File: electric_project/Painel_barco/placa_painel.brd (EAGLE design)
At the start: 60 x 100 mm, 15 parts, among them IC1 7805TV

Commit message: up
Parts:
- removed R3, R4: (no value), rcl:0204/7
- removed X2: (no value), con-molex-micro-fit-3_0:43045-1012
- added BB, BE: (no value), con-ptr500:AK500/3
- added BB_IN, BE_IN, DMS: (no value), con-ptr500:AK500/2
- added MOTOR_CON: (no value), con-molex-micro-fit-3_0:43045-1012
- moved R2 22.8 mm to (40.8, 41.0), turned to 270 degrees
- moved IC2 16.6 mm to (30.5, 50.8), turned to 0 degrees
- moved C2 4.58 mm to (33.0, 67.3)
- moved R1 4.02 mm to (22.9, 33.0), turned to 270 degrees
- moved X3 3.81 mm to (9.40, 53.7)
- moved X7 3.81 mm to (9.40, 65.8)
- moved C1 3.59 mm to (24.1, 67.3)
- moved IC1 1.80 mm to (26.7, 76.2)
- moved REV 1.80 mm to (52.1, 39.4)
- moved ON_OFF 1.27 mm to (52.1, 25.4)
- moved POT 1.27 mm to (52.1, 10.2)
- renumbered X1 to TELE_CON
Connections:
- removed net BB_IN: TELE_CON.P$12
- removed net BE_IN: TELE_CON.P$1
- removed net DMS_IN: TELE_CON.P$7
- removed net N$8: R3.1, R4.2
- new net BB_AUTO: BB.1, BB_IN.2
- new net BB_RET: BB.2, BB_IN.1, TELE_CON.P$12
- new net BE_AUTO: BE.1, BE_IN.2
- new net BE_RET: BE.2, BE_IN.1, TELE_CON.P$1
- new net WHITE_DMS: DMS.2, MOTOR_CON.P$1, TELE_CON.P$7
- net 21: now also X7.P$4; no longer X7.P$3
- net 22: now also X7.P$2; no longer X7.P$4
- net BLACK_GND: now also MOTOR_CON.P$10, MOTOR_CON.P$8; no longer X2.P$10, X2.P$8
- net BLUE_5V: now also MOTOR_CON.P$6; no longer X2.P$6
- net BROWN_REVERSE: now also MOTOR_CON.P$2; no longer X2.P$2
- net GND: now also DMS.1, MOTOR_CON.P$4, MOTOR_CON.P$5; no longer R4.1, X2.P$4, X2.P$5
- net PURP_45V_ONOFF_BACK: now also MOTOR_CON.P$3; no longer R3.2, X2.P$3
- net RED_ONOFF_45V_PH: now also MOTOR_CON.P$9; no longer X2.P$9
- net VCC_12: now also BB.3, BE.3
- net VCC_5V: now also X7.P$3; no longer X7.P$2
- net WHITE_CRUISE: no longer X2.P$1
- net YEL_POT_MEASURE: now also MOTOR_CON.P$7; no longer X2.P$7
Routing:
- net GND: track 0.00 -> 250.3 mm
- net BE_RET: track 0.00 -> 246.9 mm
- net BB_RET: track 0.00 -> 213.9 mm
- net WHITE_DMS: track 0.00 -> 165.0 mm
- net VCC_12: track 0.00 -> 118.5 mm
- net BLACK_GND: track 0.00 -> 89.7 mm
- net BROWN_REVERSE: track 0.00 -> 74.1 mm
- net BE_AUTO: track 0.00 -> 58.7 mm
- net ONOFF_MOTOR: track 0.00 -> 56.6 mm
- net PURP_45V_ONOFF_BACK: track 0.00 -> 54.4 mm
- net BB_AUTO: track 0.00 -> 50.5 mm
- net VCC_5V: track 0.00 -> 43.8 mm
- net 21: track 0.00 -> 41.2 mm
- net RED_ONOFF_45V_PH: track 0.00 -> 39.0 mm
- net BLUE_5V: track 0.00 -> 36.3 mm
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
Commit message: up
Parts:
- moved TELE_CON 3.81 mm to (9.40, 36.1)
- moved MOTOR_CON 1.27 mm to (13.2, 13.5)
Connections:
- removed net GND: C1.-, C2.-, DMS.1, IC1.2, IC2.7, MOTOR_CON.P$4, MOTOR_CON.P$5, R2.1, REV.1, X3.P$1, X7.P$1
- removed net N$1: TELE_CON.P$5
- removed net N$2: TELE_CON.P$3
- net 21: now also TELE_CON.P$3
- net 22: now also TELE_CON.P$5
- net BLACK_GND: now also C1.-, C2.-, DMS.1, IC1.2, IC2.7, MOTOR_CON.P$3, MOTOR_CON.P$4, MOTOR_CON.P$5, R2.1, REV.1, X3.P$1, X7.P$1; no longer MOTOR_CON.P$10
- net BROWN_REVERSE: now also MOTOR_CON.P$1; no longer MOTOR_CON.P$2
- net PURP_45V_ONOFF_BACK: now also MOTOR_CON.P$10; no longer MOTOR_CON.P$3
- net WHITE_DMS: now also MOTOR_CON.P$2; no longer MOTOR_CON.P$1
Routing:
- net GND: track 250.3 -> 0.00 mm
- net BLACK_GND: track 89.7 -> 257.4 mm
- net BE_RET: track 246.9 -> 127.3 mm, vias 0 -> 2
- net BB_RET: track 213.9 -> 99.5 mm, vias 0 -> 2
- net YEL_POT_MEASURE: track 36.3 -> 81.4 mm, vias 0 -> 2
- net PURP_45V_ONOFF_BACK: track 54.4 -> 43.1 mm
- net VCC_12: track 118.5 -> 108.8 mm
- net 21: track 41.2 -> 48.3 mm
- net WHITE_DMS: track 165.0 -> 159.3 mm
- net BROWN_REVERSE: track 74.1 -> 69.9 mm
- net 22: track 27.2 -> 31.2 mm
- net ONOFF_MOTOR: track 56.6 -> 54.1 mm
- net BLUE_5V: track 36.3 -> 37.0 mm
- net RED_ONOFF_45V_PH: track 39.0 -> 38.5 mm

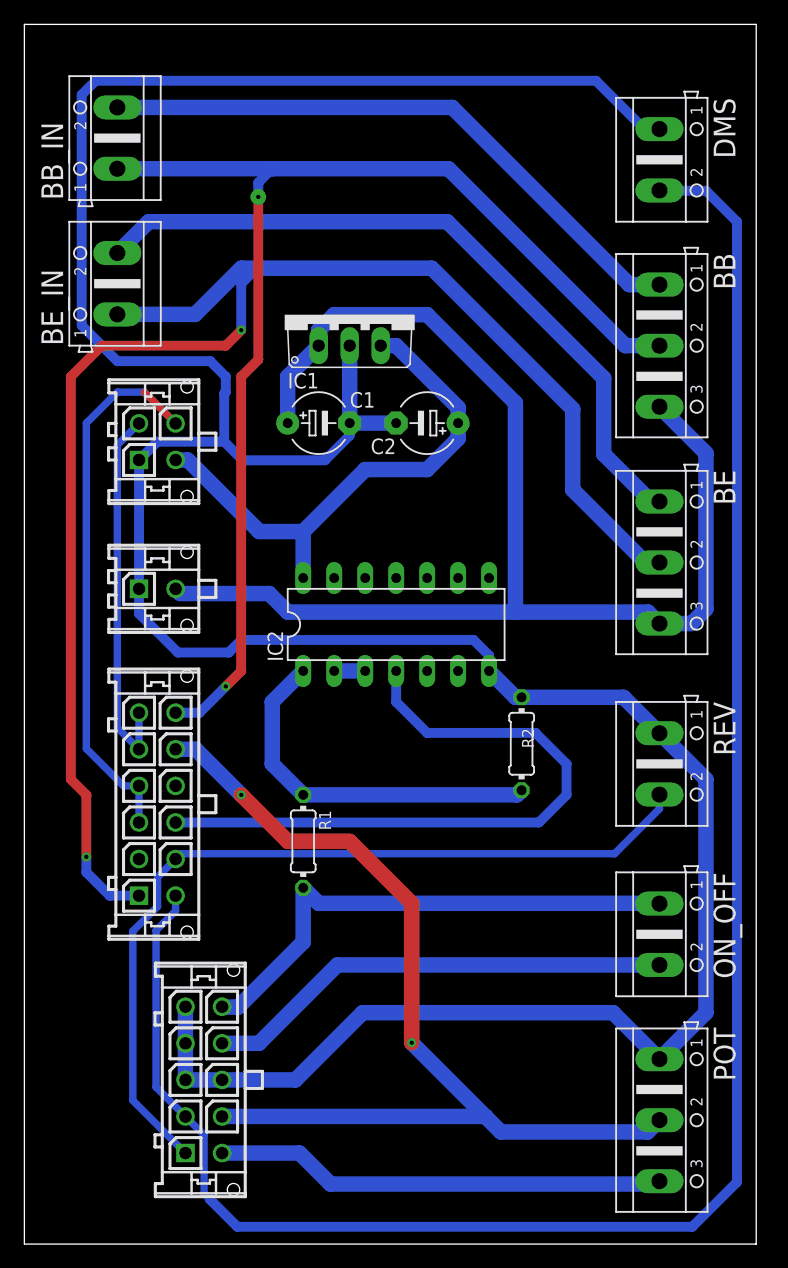
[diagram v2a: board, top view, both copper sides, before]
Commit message: increased of vias diameter
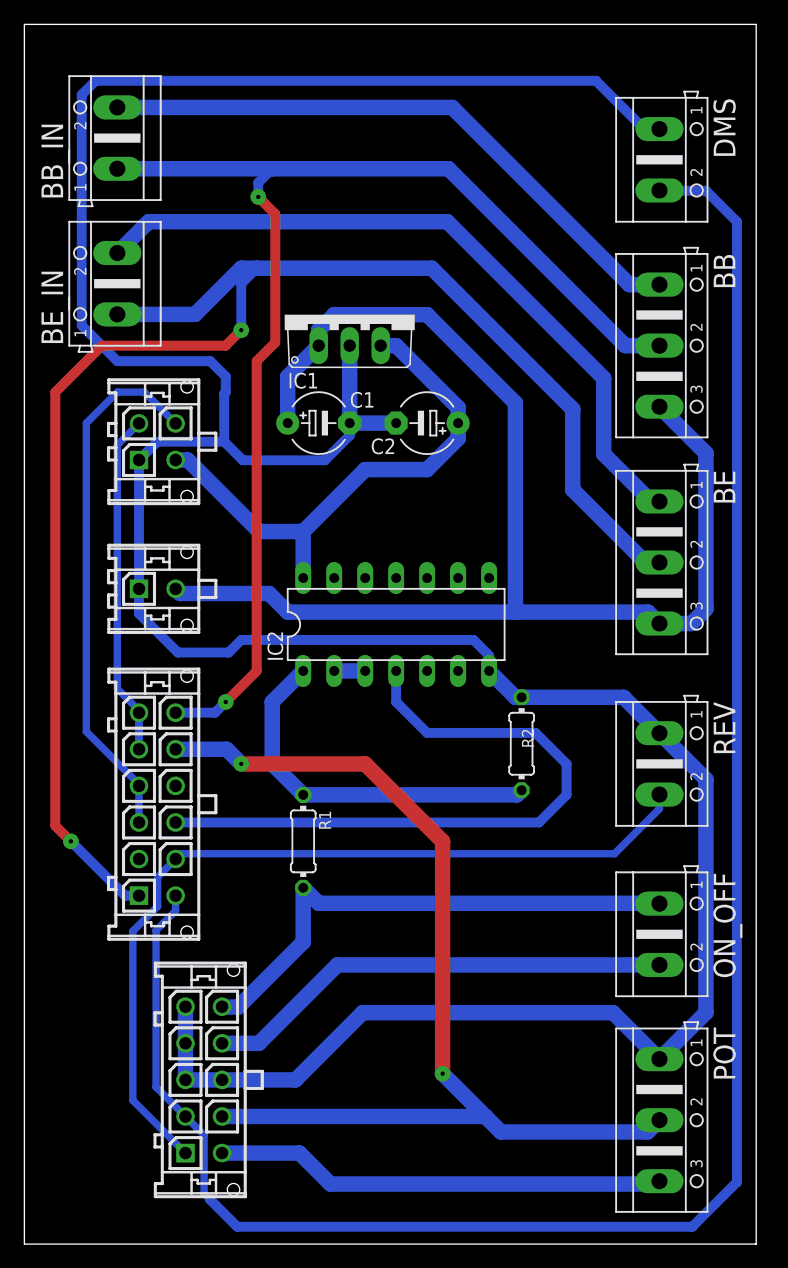
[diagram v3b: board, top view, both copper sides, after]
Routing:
- net YEL_POT_MEASURE: track 81.4 -> 85.8 mm
- net 21: track 48.3 -> 44.0 mm
- net BB_RET: track 99.5 -> 101.4 mm
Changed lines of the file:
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@@
 <?xml version="1.0" encoding="utf-8"?>
 <!DOCTYPE eagle SYSTEM "eagle.dtd">
-<eagle version="9.4.2">
+<eagle version="9.5.0">
 <drawing>
 <settings>
-<setting alwaysvectorfont="yes"/>
+<setting alwaysvectorfont="no"/>
 <setting verticaltext="up"/>
 </settings>
@@
 <contactref element="TELE_CON" pad="P$5"/>
 <wire x1="9.398" y1="40.568" x2="9.398" y2="43.568" width="0.6096" layer="16"/>
-<wire x1="9.398" y1="40.568" x2="7.62" y2="42.346" width="0.6096" layer="16"/>
+<wire x1="9.398" y1="40.568" x2="9.398" y2="43.743" width="0.6096" layer="16"/>
+<wire x1="9.398" y1="43.743" x2="7.62" y2="45.521" width="0.6096" layer="16"/>
 <wire x1="7.62" y1="65.508" x2="9.398" y2="67.286" width="0.6096" layer="16"/>
-<wire x1="7.62" y1="42.346" x2="7.62" y2="65.508" width="0.6096" layer="16"/>
+<wire x1="7.62" y1="45.521" x2="7.62" y2="65.508" width="0.6096" layer="16"/>
 </signal>
 <signal name="21">
 <contactref element="TELE_CON" pad="P$4"/>
 <contactref element="X7" pad="P$4"/>
-<wire x1="9.834" y1="69.85" x2="12.398" y2="67.286" width="0.6096" layer="1"/>
 <contactref element="TELE_CON" pad="P$3"/>
+<wire x1="9.834" y1="69.85" x2="7.62" y2="69.85" width="0.6096" layer="16"/>
+<wire x1="9.398" y1="37.568" x2="9.398" y2="37.695" width="0.6096" layer="16"/>
+<wire x1="9.398" y1="37.695" x2="5.08" y2="42.013" width="0.6096" layer="16"/>
+<wire x1="7.62" y1="69.85" x2="5.08" y2="67.31" width="0.6096" layer="16"/>
+<wire x1="5.08" y1="67.31" x2="5.08" y2="42.013" width="0.6096" layer="16"/>
+<wire x1="9.398" y1="34.568" x2="9.398" y2="37.568" width="0.6096" layer="16"/>
 <wire x1="12.398" y1="67.286" x2="9.834" y2="69.85" width="0.6096" layer="16"/>
-<wire x1="9.834" y1="69.85" x2="7.62" y2="69.85" width="0.6096" layer="16"/>
-<wire x1="8.128" y1="37.568" x2="9.398" y2="37.568" width="0.6096" layer="16"/>
-<wire x1="8.128" y1="37.568" x2="5.08" y2="40.616" width="0.6096" layer="16"/>
-<wire x1="7.62" y1="69.85" x2="5.08" y2="67.31" width="0.6096" layer="16"/>
-<wire x1="5.08" y1="67.31" x2="5.08" y2="40.616" width="0.6096" layer="16"/>
-<wire x1="9.398" y1="34.568" x2="9.398" y2="37.568" width="0.6096" layer="16"/>
 </signal>
 <signal name="EXTRA2">
@@
 <wire x1="51.102" y1="9.192" x2="39.068" y2="9.192" width="1.27" layer="16"/>
 <wire x1="37.798" y1="10.462" x2="16.51" y2="10.462" width="1.27" layer="16"/>
-<wire x1="12.398" y1="40.568" x2="14.042" y2="40.568" width="1.27" layer="16"/>
-<wire x1="14.042" y1="40.568" x2="17.78" y2="36.83" width="1.27" layer="16"/>
-<via x="17.78" y="36.83" extent="1-16" drill="0.35"/>
-<wire x1="17.78" y1="36.83" x2="21.59" y2="33.02" width="1.27" layer="1"/>
-<wire x1="31.75" y1="27.94" x2="31.75" y2="16.51" width="1.27" layer="1"/>
-<via x="31.75" y="16.51" extent="1-16" drill="0.35"/>
-<wire x1="31.75" y1="16.51" x2="37.798" y2="10.462" width="1.27" layer="16"/>
+<wire x1="12.398" y1="40.568" x2="16.582" y2="40.568" width="1.27" layer="16"/>
+<wire x1="16.582" y1="40.568" x2="17.78" y2="39.37" width="1.27" layer="16"/>
+<via x="17.78" y="39.37" extent="1-16" drill="0.35" diameter="1.3"/>
+<wire x1="34.29" y1="33.02" x2="34.29" y2="13.97" width="1.27" layer="1"/>
+<via x="34.29" y="13.97" extent="1-16" drill="0.35" diameter="1.3"/>
+<wire x1="34.29" y1="13.97" x2="37.798" y2="10.462" width="1.27" layer="16"/>
 <wire x1="37.798" y1="10.462" x2="39.068" y2="9.192" width="1.27" layer="16"/>
-<wire x1="21.59" y1="33.02" x2="26.67" y2="33.02" width="1.27" layer="1"/>
-<wire x1="26.67" y1="33.02" x2="31.75" y2="27.94" width="1.27" layer="1"/>
+<wire x1="27.94" y1="39.37" x2="17.78" y2="39.37" width="1.27" layer="1"/>
+<wire x1="27.94" y1="39.37" x2="34.29" y2="33.02" width="1.27" layer="1"/>
 </signal>
 <signal name="WHITE_CRUISE">
@@
 <wire x1="49.276" y1="73.66" x2="52.07" y2="73.66" width="1.27" layer="16"/>
 <wire x1="34.7726" y1="88.1634" x2="49.276" y2="73.66" width="1.27" layer="16"/>
-<wire x1="12.398" y1="43.568" x2="14.358" y2="43.568" width="0.8128" layer="16"/>
-<via x="16.51" y="45.72" extent="1-16" drill="0.35"/>
-<wire x1="16.51" y1="45.72" x2="17.78" y2="46.99" width="0.8128" layer="1"/>
-<wire x1="17.78" y1="71.12" x2="17.78" y2="46.99" width="0.8128" layer="1"/>
-<wire x1="19.177" y1="72.517" x2="19.177" y2="85.852" width="0.8128" layer="1"/>
+<wire x1="12.398" y1="43.568" x2="15.628" y2="43.568" width="0.8128" layer="16"/>
+<via x="16.51" y="44.45" extent="1-16" drill="0.35" diameter="1.3"/>
+<wire x1="16.51" y1="44.45" x2="19.05" y2="46.99" width="0.8128" layer="1"/>
+<wire x1="19.05" y1="72.39" x2="19.05" y2="46.99" width="0.8128" layer="1"/>
+<wire x1="20.574" y1="84.455" x2="20.574" y2="73.914" width="0.8128" layer="1"/>
+<wire x1="20.574" y1="84.455" x2="19.177" y2="85.852" width="0.8128" layer="1"/>
 <via x="19.177" y="85.852" extent="1-16" drill="0.35" diameter="1.3"/>
 <wire x1="19.177" y1="85.852" x2="19.177" y2="87.0204" width="0.8128" layer="16"/>
 <wire x1="19.177" y1="87.0204" x2="20.32" y2="88.1634" width="0.8128" layer="16"/>
-<wire x1="14.358" y1="43.568" x2="16.51" y2="45.72" width="0.8128" layer="16"/>
-<wire x1="17.78" y1="71.12" x2="19.177" y2="72.517" width="0.8128" layer="1"/>
+<wire x1="15.628" y1="43.568" x2="16.51" y2="44.45" width="0.8128" layer="16"/>
+<wire x1="19.05" y1="72.39" x2="20.574" y2="73.914" width="0.8128" layer="1"/>
 </signal>
 <signal name="BE_RET">
@@
 <contactref element="BE" pad="2"/>
 <contactref element="TELE_CON" pad="P$1"/>
-<wire x1="9.398" y1="28.568" x2="6.992" y2="28.568" width="0.8128" layer="16"/>
-<wire x1="5.08" y1="30.48" x2="5.08" y2="31.75" width="0.8128" layer="16"/>
-<via x="5.08" y="31.75" extent="1-16" drill="0.35"/>
-<wire x1="6.992" y1="28.568" x2="5.08" y2="30.48" width="0.8128" layer="16"/>
+<wire x1="9.398" y1="28.568" x2="8.262" y2="28.568" width="0.8128" layer="16"/>
+<via x="3.81" y="33.02" extent="1-16" drill="0.35" diameter="1.3"/>
+<wire x1="8.262" y1="28.568" x2="3.81" y2="33.02" width="0.8128" layer="16"/>
 <wire x1="7.62" y1="76.2254" x2="13.9954" y2="76.2254" width="1.27" layer="16"/>
 <wire x1="13.9954" y1="76.2254" x2="17.78" y2="80.01" width="1.27" layer="16"/>
@@
 <wire x1="50.927" y1="55.88" x2="52.07" y2="55.88" width="1.27" layer="16"/>
 <wire x1="33.401" y1="80.01" x2="44.958" y2="68.453" width="1.27" layer="16"/>
-<wire x1="5.08" y1="31.75" x2="5.08" y2="36.83" width="0.8128" layer="1"/>
-<wire x1="5.08" y1="36.83" x2="3.81" y2="38.1" width="0.8128" layer="1"/>
-<wire x1="3.81" y1="38.1" x2="3.81" y2="71.12" width="0.8128" layer="1"/>
-<wire x1="3.81" y1="71.12" x2="6.35" y2="73.66" width="0.8128" layer="1"/>
+<wire x1="3.81" y1="33.02" x2="2.54" y2="34.29" width="0.8128" layer="1"/>
+<wire x1="2.54" y1="34.29" x2="2.54" y2="69.85" width="0.8128" layer="1"/>
+<wire x1="2.54" y1="69.85" x2="6.35" y2="73.66" width="0.8128" layer="1"/>
 <wire x1="6.35" y1="73.66" x2="16.51" y2="73.66" width="0.8128" layer="1"/>
 <wire x1="16.51" y1="73.66" x2="17.78" y2="74.93" width="0.8128" layer="1"/>
-<via x="17.78" y="74.93" extent="1-16" drill="0.35"/>
+<via x="17.78" y="74.93" extent="1-16" drill="0.35" diameter="1.3"/>
 <wire x1="17.78" y1="74.93" x2="17.78" y2="78.74" width="0.8128" layer="16"/>
 <wire x1="17.78" y1="78.74" x2="19.05" y2="80.01" width="0.8128" layer="16"/>
